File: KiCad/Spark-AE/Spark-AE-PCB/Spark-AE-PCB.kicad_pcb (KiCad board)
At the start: 2 copper layers, 50 x 100 mm, 100 parts, among them J1 Conn_01x20_Socket, J2 Conn_01x20_Socket, J3 AE_BUS, J4 Inputs, J5 Outputs, J6 I2C_IN, J7 I2C_OUT, J8 Conn_02x06_Top_Bottom, Q1 2N3904, Q2 2N3904, SW1 SW_Push, SW2 SW_Push, U2 MCP6002-xMS, U3 Driver_LED_PCA9633PW,118, U4 MCP6002-xMS, U5 MCP6002-xMS, U6 Connector_Micro_SD_Card_Yamai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, U7 MCP6002-xMS, U8 74LVC1G125

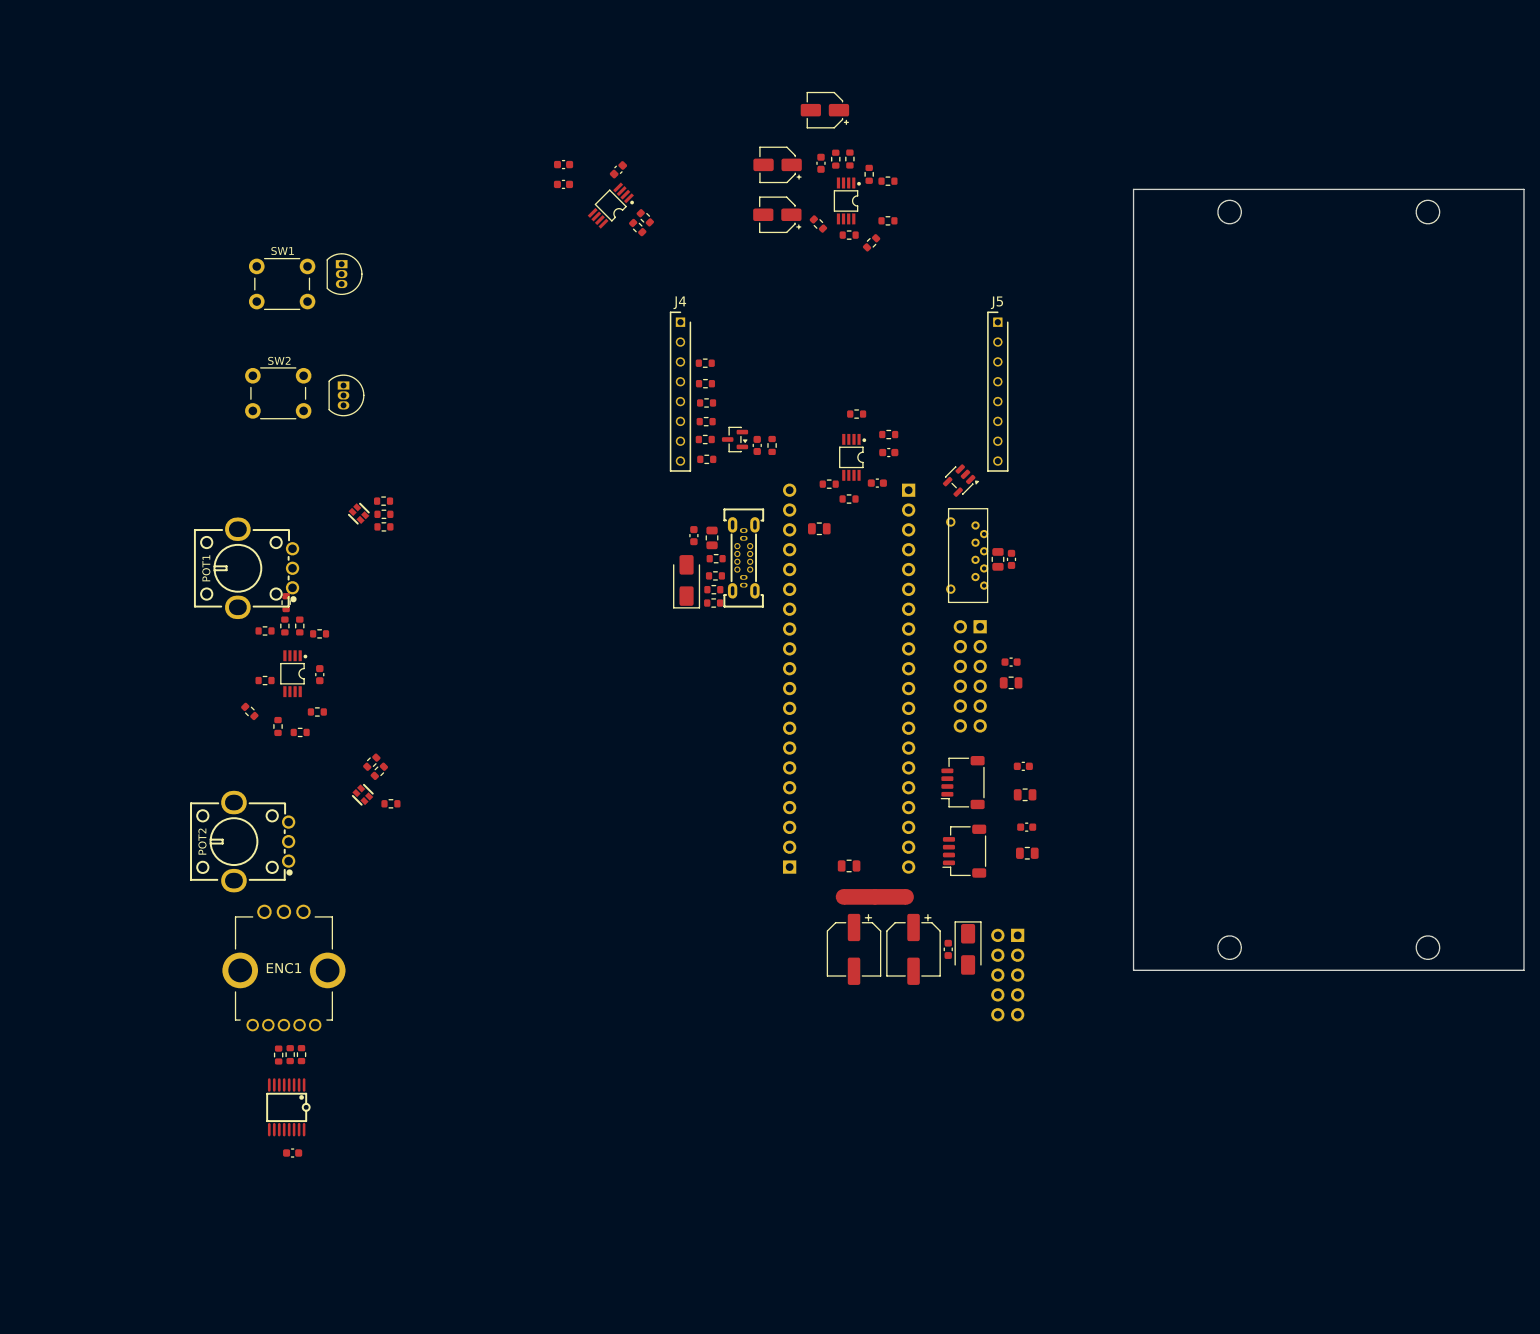
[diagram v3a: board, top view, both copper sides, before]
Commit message: schematic 100% complete. pcb layout around 50% complete.
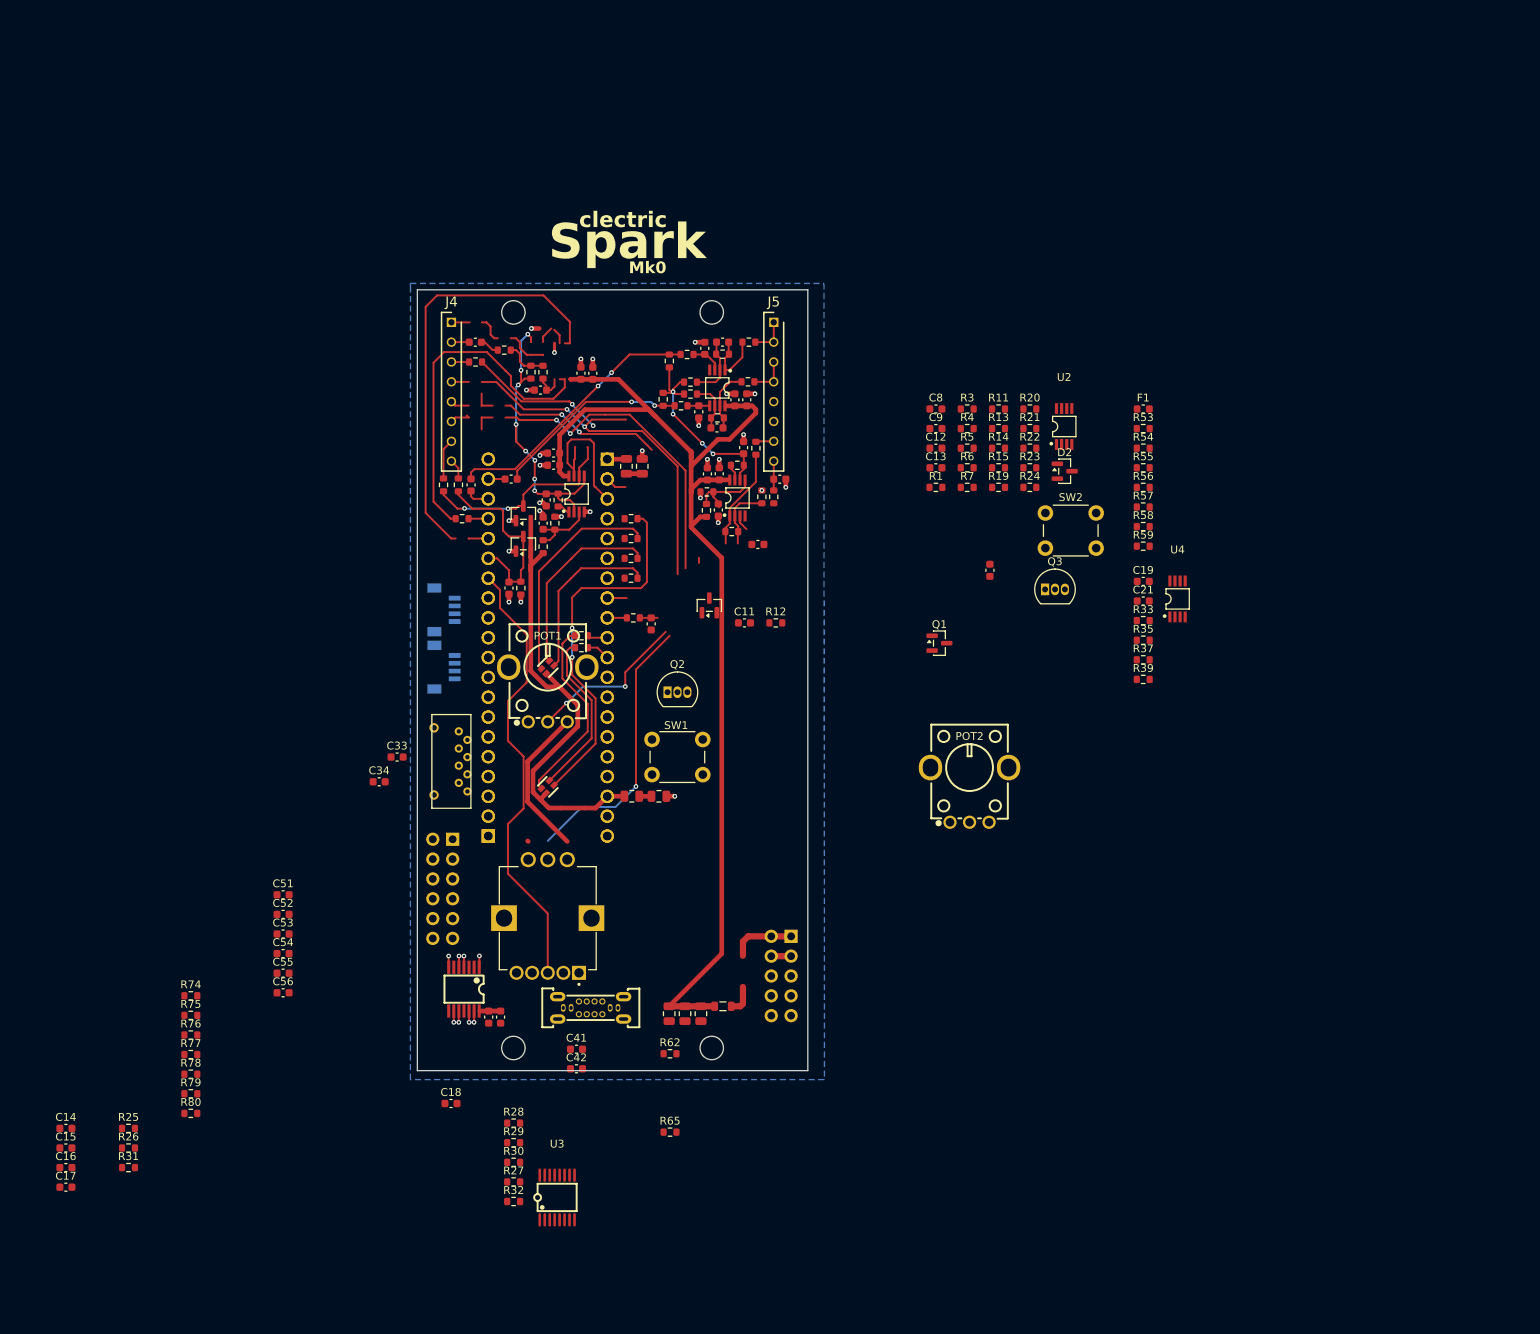
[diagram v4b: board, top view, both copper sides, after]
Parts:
- removed ENC1: RotaryEncoder_Switch_Bourns_PEL12T-4225S-S1024, clectric-diy:RotaryEncoder_Switch_Bourns_PEL12T-4225S-S1024
- removed J7: I2C_OUT, Connector_JST:JST_SH_SM04B-SRSS-TB_1x04-1MP_P1.00mm_Horizontal
- removed J8: Conn_02x06_Top_Bottom, Connector_PinHeader_2.54mm:PinHeader_2x06_P2.54mm_Vertical
- removed NT1: NetTie_3_Tee, NetTie:NetTie-3_SMD_Pad2.0mm
- added C27: 1nF, Capacitor_SMD:C_0603_1608Metric, F.Cu at (115.2, 53.6)
- added C28: 1nF, Capacitor_SMD:C_0603_1608Metric, F.Cu at (114.4, 61.8)
- added C29: 680pF, Capacitor_SMD:C_0603_1608Metric, F.Cu at (117.5, 52.8)
- added C30: 680pF, Capacitor_SMD:C_0603_1608Metric, F.Cu at (116.7, 63.8)
- added C31: 100nF, Capacitor_SMD:C_0603_1608Metric, F.Cu at (120.6, 60.2)
- added C32: 10uF, Capacitor_SMD:C_0603_1608Metric, F.Cu at (119.0, 60.2)
- added C33: 10uF, Capacitor_SMD:C_0603_1608Metric, F.Cu at (75.8, 106.0)
- added C34: 100nF, Capacitor_SMD:C_0603_1608Metric, F.Cu at (73.5, 109.1)
- added C35: 100nF, Capacitor_SMD:C_0603_1608Metric, F.Cu at (94.5, 76.0)
- added C36: 100nF, Capacitor_SMD:C_0603_1608Metric, F.Cu at (94.9, 73.1)
- added C37: 100nF, Capacitor_SMD:C_0603_1608Metric, F.Cu at (95.8, 68.6)
- added C38: 10uF, Capacitor_SMD:C_0603_1608Metric, F.Cu at (95.8, 67.1)
- added C39: 10nF, Capacitor_SMD:C_0603_1608Metric, F.Cu at (108.3, 88.9)
- added C40: 1nF, Capacitor_SMD:C_0603_1608Metric, F.Cu at (122.0, 78.8)
- added C41: 100nF, Capacitor_SMD:C_0603_1608Metric, F.Cu at (98.8, 143.4)
- added C42: 10uF, Capacitor_SMD:C_0603_1608Metric, F.Cu at (98.8, 145.9)
- added C43: 100nF, Capacitor_SMD:C_0603_1608Metric, F.Cu at (117.0, 69.7)
- added C44: 10uF, Capacitor_SMD:C_0603_1608Metric, F.Cu at (115.5, 69.7)
- added C45: 10pF, Capacitor_SMD:C_0603_1608Metric, F.Cu at (124.8, 70.4)
- added C46: 100nF, Capacitor_SMD:C_0603_1608Metric, F.Cu at (116.9, 74.3)
- added C47: 100pF, Capacitor_SMD:C_0603_1608Metric, F.Cu at (90.1, 84.3)
- added C48: 100nF, Capacitor_SMD:C_0603_1608Metric, F.Cu at (120.2, 66.4)
- added C49: 100nF, Capacitor_SMD:C_0603_1608Metric, F.Cu at (87.5, 139.3)
- added C50: 10uF, Capacitor_SMD:C_0603_1608Metric, F.Cu at (89.0, 139.3)
- added C51: 100nF, Capacitor_SMD:C_0603_1608Metric, F.Cu at (61.2, 123.6)
- added C52: 10uF, Capacitor_SMD:C_0603_1608Metric, F.Cu at (61.2, 126.1)
- added C53: 100nF, Capacitor_SMD:C_0603_1608Metric, F.Cu at (61.2, 128.6)
- added C54: 10uF, Capacitor_SMD:C_0603_1608Metric, F.Cu at (61.2, 131.1)
- added C55: 100nF, Capacitor_SMD:C_0603_1608Metric, F.Cu at (61.2, 133.7)
- added C56: 10uF, Capacitor_SMD:C_0603_1608Metric, F.Cu at (61.2, 136.2)
- added CN1: I2C_IN, clectric-diy:Connector_JST_BM04B-SRSS-TBT-LF-SN, B.Cu at (81.9, 87.1)
- added CN2: I2C_OUT, clectric-diy:Connector_JST_BM04B-SRSS-TBT-LF-SN, B.Cu at (81.8, 94.5)
- added D4: BAT54S, Package_TO_SOT_SMD:SOT-23, F.Cu at (91.9, 74.8)
- added D5: BAT54S, Package_TO_SOT_SMD:SOT-23, F.Cu at (91.9, 78.7)
- added F1: nSMD050-33V, Fuse:Fuse_0603_1608Metric, F.Cu at (171.3, 61.4)
- added Q3: 2N3904, Package_TO_SOT_THT:TO-92_Inline, F.Cu at (158.8, 84.5)
- added R11: 10K, Resistor_SMD:R_0603_1608Metric, F.Cu at (152.8, 61.4)
- added R22: 10K, Resistor_SMD:R_0603_1608Metric, F.Cu at (156.8, 66.4)
- added R47: 15K, Resistor_SMD:R_0603_1608Metric, F.Cu at (117.5, 54.4)
- added R48: 15K, Resistor_SMD:R_0603_1608Metric, F.Cu at (116.8, 62.5)
- added R49: 1K, Resistor_SMD:R_0603_1608Metric, F.Cu at (120.8, 52.8)
- added R50: 1K, Resistor_SMD:R_0603_1608Metric, F.Cu at (120.7, 57.9)
- added R51: 10K, Resistor_SMD:R_0603_1608Metric, F.Cu at (94.5, 79.0)
- added R52: 10K, Resistor_SMD:R_0603_1608Metric, F.Cu at (96.0, 76.0)
- added R53: 10K, Resistor_SMD:R_0603_1608Metric, F.Cu at (171.3, 63.9)
- added R54: 20K, Resistor_SMD:R_0603_1608Metric, F.Cu at (171.3, 66.4)
- added R55: 47K, Resistor_SMD:R_0603_1608Metric, F.Cu at (171.3, 68.9)
- added R56: 47K, Resistor_SMD:R_0603_1608Metric, F.Cu at (171.3, 71.4)
- added R57: 47K, Resistor_SMD:R_0603_1608Metric, F.Cu at (171.3, 74.0)
- added R58: 47K, Resistor_SMD:R_0603_1608Metric, F.Cu at (171.3, 76.5)
- added R59: 47K, Resistor_SMD:R_0603_1608Metric, F.Cu at (171.3, 79.0)
- added R60: 100R, Resistor_SMD:R_0603_1608Metric, F.Cu at (96.4, 73.1)
- added R61: 1K, Resistor_SMD:R_0603_1608Metric, F.Cu at (81.7, 71.1)
- added R62: 10K, Resistor_SMD:R_0603_1608Metric, F.Cu at (110.7, 144.0)
- added R63: 10K, Resistor_SMD:R_0603_1608Metric, F.Cu at (106.0, 88.2)
- added R64: 12.7K, Resistor_SMD:R_0603_1608Metric, F.Cu at (122.5, 72.7)
- added R65: 10K, Resistor_SMD:R_0603_1608Metric, F.Cu at (110.7, 154.0)
- added R66: 10K, Resistor_SMD:R_0603_1608Metric, F.Cu at (118.6, 77.1)
- added R67: 1K, Resistor_SMD:R_0603_1608Metric, F.Cu at (121.7, 66.4)
- added R68: 10K, Resistor_SMD:R_0603_1608Metric, F.Cu at (115.4, 74.4)
- added R69: 10K, Resistor_SMD:R_0603_1608Metric, F.Cu at (115.5, 72.0)
- added R70: 1K, Resistor_SMD:R_0603_1608Metric, F.Cu at (124.0, 72.7)
- added R71: 10K, Resistor_SMD:R_0603_1608Metric, F.Cu at (83.6, 71.1)
- added R72: 470R, Resistor_SMD:R_0603_1608Metric, F.Cu at (91.6, 84.3)
- added R73: 100R, Resistor_SMD:R_0603_1608Metric, F.Cu at (119.4, 68.6)
- added R74: 100R, Resistor_SMD:R_0603_1608Metric, F.Cu at (49.4, 136.5)
- added R75: 100R, Resistor_SMD:R_0603_1608Metric, F.Cu at (49.4, 139.1)
- added R76: 10K, Resistor_SMD:R_0603_1608Metric, F.Cu at (49.4, 141.6)
- added R77: 47R, Resistor_SMD:R_0603_1608Metric, F.Cu at (49.4, 144.1)
- added R78: 47R, Resistor_SMD:R_0603_1608Metric, F.Cu at (49.4, 146.6)
- added R79: 47R, Resistor_SMD:R_0603_1608Metric, F.Cu at (49.4, 149.1)
- added R80: 47R, Resistor_SMD:R_0603_1608Metric, F.Cu at (49.4, 151.6)
- added U1: Daisy_Seed, clectric-diy:MCU_Module_Electrosmith_DAISY_SEED, B.Cu at (87.5, 116.1)
- added U9: 74xx_Nexperia_74HCT125PW_118, clectric-diy:74xx_Nexperia_74HCT125PW_118, F.Cu at (84.3, 135.7)
- C1: value 220uF -> 100uF; footprint Capacitor_SMD:CP_Elec_6.3x5.4 -> Capacitor_SMD:C_0805_2012Metric
- C10: value 10uF -> 100nF; footprint Capacitor_SMD:CP_Elec_4x5.4 -> Capacitor_SMD:C_0603_1608Metric
- C11: footprint Capacitor_SMD:CP_Elec_4x5.4 -> Capacitor_SMD:C_0603_1608Metric
- C13: value 10uF -> 10nF; footprint Capacitor_SMD:CP_Elec_4x5.4 -> Capacitor_SMD:C_0603_1608Metric
- C14: value 10uF -> 10nF; footprint Capacitor_SMD:C_0805_2012Metric -> Capacitor_SMD:C_0603_1608Metric
- C15, C9: value 100nF -> 10nF
- C17, C25: value 100nF -> 10uF
- C19: value 100nF -> 1uF
- C2: value 220uF -> 10uF; footprint Capacitor_SMD:CP_Elec_6.3x5.4 -> Capacitor_SMD:C_0805_2012Metric
- C20: value 10uF -> 1uF; footprint Capacitor_SMD:C_0805_2012Metric -> Capacitor_SMD:C_0603_1608Metric
- C21: value 100nF -> 220pF
- C22: value 10uF -> 220pF; footprint Capacitor_SMD:C_0805_2012Metric -> Capacitor_SMD:C_0603_1608Metric
- C24, C26: footprint Capacitor_SMD:C_0805_2012Metric -> Capacitor_SMD:C_0603_1608Metric
- C3: value 10uF -> 100nF
- C5: footprint Capacitor_SMD:C_0603_1608Metric -> Capacitor_SMD:C_0805_2012Metric
- C6: value 100nF -> 10uF; footprint Capacitor_SMD:C_0603_1608Metric -> Capacitor_SMD:C_0805_2012Metric
- C7: value 1uF -> 100nF; footprint Capacitor_SMD:C_0603_1608Metric -> Capacitor_SMD:C_0805_2012Metric
- C8: value 1uF -> 100nF
- D1: value SS14 -> BAT54S; footprint Diode_SMD:D_SMA -> Package_TO_SOT_SMD:SOT-23
- D3: value 2214 -> RotaryEncoder_Switch_Bourns_PEL12T-4225S-S1024; footprint Diode_SMD:D_SMA -> clectric-diy:RotaryEncoder_Switch_Bourns_PEL12T-4225S-S1024
- FB1: value BLM18AG601 -> FerriteBead; footprint Inductor_SMD:L_0603_1608Metric -> Inductor_SMD:L_0805_2012Metric
- J6: value I2C_IN -> Conn_02x06_Top_Bottom; footprint Connector_JST:JST_SH_SM04B-SRSS-TB_1x04-1MP_P1.00mm_Horizontal -> Connector_PinHeader_2.54mm:PinHeader_2x06_P2.54mm_Vertical; moved to B.Cu
- Q1: value 2N3904 -> AO3401; footprint Package_TO_SOT_THT:TO-92_Inline -> Package_TO_SOT_SMD:SOT-23
- R1, R13, R38: value 1K8 -> 10K
- R10, R18: value 100K -> 47R
- R12: value 10K -> 1K
- R14, R41, R42, R6: value 1K -> 100K
- R15, R25, R7: value 100R -> 10K
- R16, R8: value 100R -> 47R
- R17: value 3K3 -> 330R
- R19: value 100K -> 10K
- R2: value 3K3 -> 10K
- R23: value 1K -> 10K
- R24: value 100R -> 1K
- R26: value 4K7 -> 10K
- R28: value 100K -> 680R
- R29: value 100K -> 470R
- R30: value 10K -> 470R
- R32: value 100K -> 4K7
- R33: value 100K -> 150K
- R34: value 15K -> 150K
- R35: value 15K -> 100K
- R36: value 10K -> 100K
- R39: value 3K3 -> 1K
- R40: value 5K1 -> 1K
- R45, R46: value 5K1 -> 10K
- R9: value 100K -> 330R
- U2, U4, U5: value MCP6002-xMS -> MCP6002T-I_MS
- U6: value Connector_Micro_SD_Card_Yamaichi_PJS008U-3000-0 -> MCP6002T-I_MS; footprint clectric-diy:PJS008U-3000-0 -> clectric-diy:Amplifier_Operational_Microchip_MCP6002T-I_MS
- U7: value MCP6002-xMS -> Connector_Micro_SD_Card_Yamaichi_PJS008U-3000-0; footprint clectric-diy:Amplifier_Operational_Microchip_MCP6002T-I_MS -> clectric-diy:PJS008U-3000-0
- U8: value 74LVC1G125 -> MCP6002T-I_MS; footprint Package_TO_SOT_SMD:SOT-23-5 -> clectric-diy:Amplifier_Operational_Microchip_MCP6002T-I_MS
- moved R31 149.7 mm to (41.4, 158.5), turned to 0 degrees
- moved C15 142.6 mm to (33.4, 156.0), turned to 0 degrees
- moved C14 139.8 mm to (33.4, 153.5), turned to 0 degrees
- moved R32 139.2 mm to (90.7, 162.9), turned to 0 degrees
- moved C17 137.6 mm to (33.4, 161.1), turned to 0 degrees
- moved R30 134.9 mm to (90.7, 157.9), turned to 0 degrees
- moved R26 134.7 mm to (41.4, 156.0), turned to 0 degrees
- moved R28 130.8 mm to (90.7, 152.9), turned to 0 degrees
- moved C16 128.0 mm to (33.4, 158.5), turned to 0 degrees
- moved R27 124.6 mm to (90.7, 160.4), turned to 0 degrees
- moved R29 123.9 mm to (90.7, 155.4), turned to 0 degrees
- moved R23 119.8 mm to (156.8, 68.9), turned to 0 degrees
- moved R24 119.4 mm to (156.8, 71.4), turned to 0 degrees
- moved U2 103.8 mm to (161.2, 63.6), turned to 0 degrees
- moved R21 101.2 mm to (156.8, 63.9)
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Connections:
- C1 pad 1: 5V -> +5V
- C10 pad 1: Net-(U5A-+) -> +5V
- C10 pad 2: AUDIO_OUT_1 -> GND
- C11 pad 1: Net-(U5B-+) -> GND
- C11 pad 2: AUDIO_OUT_2 -> +5V
- C12 pad 1: GNDA -> SW2
- C12 pad 2: 5V -> GND
- C13 pad 1: 5V -> POT2
- C13 pad 2: GNDA -> GND
- C14 pad 1: 3V3_D -> ENC_A
- C14 pad 2: GNDD -> GND
- C15 pad 1: 3V3_D -> ENC_B
- C15 pad 2: GNDD -> GND
- C16 pad 1: A1_D16 -> GND
- C16 pad 2: GNDA -> ENC_CLICK
- C17 pad 1: GNDA -> +3.3V
- C17 pad 2: 5V -> GND
- C18 pad 1: GNDD -> +3.3V
- C18 pad 2: 5V -> GND
- C19 pad 1: GNDD -> AUDIO_AE_IN_1
- C19 pad 2: 5V -> Net-(C19-Pad2)
- C2 pad 1: 5V -> +5V
- C20 pad 1: GNDD -> AUDIO_AE_IN_2
- C20 pad 2: 5V -> Net-(C20-Pad2)
- C21 pad 1: 3V3_D -> Net-(U4A-+)
- C21 pad 2: GNDD -> GND
- C22 pad 1: 3V3_D -> Net-(U4B-+)
- C22 pad 2: GNDD -> GND
- C23 pad 1: 3V3_D -> GND
- C23 pad 2: GNDD -> +5V
- C24 pad 1: 3V3_D -> GND
- C24 pad 2: GNDD -> +5V
- C25 pad 1: 3V3_D -> Net-(C25-Pad1)
- C25 pad 2: GNDD -> AUDIO_OUT_1
- C26 pad 1: 3V3_D -> Net-(C26-Pad1)
- C26 pad 2: GNDD -> AUDIO_OUT_2
- C3 pad 1: 3V3_D -> +5V
- C3 pad 2: GNDD -> GND
- C4 pad 1: 3V3_A -> +3.3V
- C4 pad 2: GNDA -> Net-(C4-Pad2)
- C5 pad 1: GNDA -> Net-(C4-Pad2)
- C5 pad 2: 3V3_D -> GND
- C6 pad 1: GNDD -> +3.3VA
- C6 pad 2: 3V3_D -> Net-(C6-Pad2)
- C7 pad 1: AUDIO_AE_IN_1 -> Net-(C6-Pad2)
- C7 pad 2: Net-(U4A-+) -> GND
- C8 pad 1: AUDIO_AE_IN_2 -> SW1
- C8 pad 2: Net-(U4B-+) -> GND
- C9 pad 1: GNDA -> POT1
- C9 pad 2: 5V -> GND
- D1 pad 1: 5V -> GND
- D1 pad 2: GND -> +3.3VA
- D2 pad 1: GNDA -> GND
- D2 pad 2: 3V3_D -> +3.3VA
- D2 pad 3: A1_D16 -> POT2
- D3 pad 1: 5V -> Net-(D3-Pad1)
- D3 pad 2: GNDD -> Net-(D3-Pad2)
- FB1 pad 1: 5V -> +5V
- FB1 pad 2: GND -> /Power Regulation/VCC_PROTECT
- J1 pad 1: 3V3_A -> +3.3VA
- J1 pad 18: 3V3_D -> +3.3V
- J1 pad 19: 5V -> +5V
- J1 pad 20: GNDD -> GND
- J1 pad 3: A1_D16 -> A1
- J1 pad 9: A7_D22 -> A7
- J2 pad 20: GNDA -> GND
- J3 pad 1: 5V -> /Power Regulation/VCC_RAW
- J3 pad 2: 5V -> /Power Regulation/VCC_RAW
- J4 pad 7: A1_D16_AE_IN -> A1_AE_IN
- J5 pad 7: A7_D22_AE_OUT -> A7_AE_OUT
- J6 pad 1: 3V3_D -> Net-(J6-Pin_1)
- J6 pad 2: GNDD -> Net-(J6-Pin_2)
- J6 pad 3: I2C_SDA -> Net-(J6-Pin_3)
- J6 pad 4: I2C_SCL -> Net-(J6-Pin_4)
- LED1 pad 3: 3V3_D -> +3.3V
- LED2 pad 3: 3V3_D -> +3.3V
- POT1 pad 1: 3V3_A -> GND
- POT1 pad 3: GNDA -> +3.3VA
- POT1 pad 4: GNDA -> GND
- POT1 pad 5: GNDA -> GND
- POT2 pad 1: 3V3_A -> GND
- POT2 pad 3: GNDA -> +3.3VA
- POT2 pad 4: GNDA -> GND
- POT2 pad 5: GNDA -> GND
- Q1 pad 1: GNDD -> GND
- Q1 pad 2: Net-(Q1-B) -> /Power Regulation/VCC_PROTECT
- Q1 pad 3: SW_1 -> /Power Regulation/VCC_RAW
- Q2 pad 1: GNDD -> GND
- Q2 pad 3: SW_2 -> SW1
- R1 pad 2: Net-(R1-Pad2) -> GND
- R10 pad 1: Net-(U2A--) -> LED1_B
- R10 pad 2: POT1 -> Net-(LED1-Pad4)
- R12 pad 1: SW2_CV -> Net-(R11-Pad2)
- R12 pad 2: Net-(Q2-B) -> POT1
- R13 pad 2: Net-(R13-Pad2) -> GND
- R14 pad 1: LED2_G -> Net-(U2B-+)
- R14 pad 2: Net-(LED2-Pad1) -> POT2_CV
- R15 pad 1: LED2_B -> SW2_CV
- R15 pad 2: Net-(LED2-Pad2) -> Net-(Q3-B)
- R16 pad 1: LED2_R -> LED2_G
- R16 pad 2: Net-(LED2-Pad4) -> Net-(LED2-Pad1)
- R17 pad 1: Net-(R13-Pad2) -> LED2_R
- R17 pad 2: GNDA -> Net-(LED2-Pad2)
- R18 pad 1: Net-(R13-Pad2) -> LED2_B
- R18 pad 2: Net-(U2B-+) -> Net-(LED2-Pad4)
- R19 pad 1: GNDA -> +3.3V
- R19 pad 2: Net-(U2B--) -> SW2
- R2 pad 1: Net-(R1-Pad2) -> SW1_CV
- R2 pad 2: GNDA -> Net-(Q2-B)
- R20 pad 1: Net-(U2B-+) -> Net-(POT2-Pad2)
- R20 pad 2: Net-(POT2-Pad2) -> Net-(U2B-+)
- R21 pad 1: Net-(U2B--) -> Net-(Q3-B)
- R21 pad 2: POT2 -> GND
- R23 pad 1: Net-(ENC1--_1) -> Net-(U2B--)
- R23 pad 2: ENC_LED_RED -> Net-(R23-Pad2)
- R24 pad 1: Net-(ENC1--_2) -> Net-(R23-Pad2)
- R24 pad 2: ENC_LED_GREEN -> POT2
- R25 pad 1: Net-(ENC1-+_1) -> +3.3V
- R25 pad 2: ENC_LED_BLUE -> ENC_A
- R26 pad 1: 3V3_D -> +3.3V
- R26 pad 2: I2C_SDA -> ENC_B
- R27 pad 1: 3V3_D -> +3.3V
- R27 pad 2: I2C_SCL -> I2C_SDA
- R28 pad 1: Net-(U4B--) -> Net-(D3-Pad1)
- R28 pad 2: AUDIO_IN_2 -> ENC_LED_RED
- R29 pad 1: Net-(U4A--) -> Net-(D3-Pad2)
- R29 pad 2: AUDIO_IN_1 -> ENC_LED_GREEN
- R3 pad 1: SW1_CV -> +3.3V
- R3 pad 2: Net-(Q1-B) -> SW1
- R30 pad 1: 5V -> Net-(D3-Pad4)
- R30 pad 2: Net-(U5A--) -> ENC_LED_BLUE
- R31 pad 1: 5V -> +3.3V
- R31 pad 2: Net-(U5B--) -> ENC_CLICK
- R32 pad 1: 5V -> +3.3V
- R32 pad 2: Net-(U5A-+) -> I2C_SCL
- R33 pad 1: 5V -> Net-(C19-Pad2)
- R33 pad 2: Net-(U5B-+) -> Net-(R33-Pad2)
- R34 pad 1: Net-(U5A--) -> Net-(C20-Pad2)
- R35 pad 1: Net-(U5B--) -> Net-(R33-Pad2)
- R35 pad 2: Net-(R35-Pad2) -> VREF_1V65
- R36 pad 2: AUDIO_AE_OUT_1 -> VREF_1V65
- R37 pad 1: Net-(R35-Pad2) -> Net-(R33-Pad2)
- R37 pad 2: AUDIO_AE_OUT_2 -> Net-(U4A-+)
- R38 pad 1: A1_D16 -> Net-(R34-Pad2)
- R38 pad 2: A1_D16_AE_IN -> Net-(U4B-+)
- R39 pad 1: A1_D16 -> AUDIO_IN_1
- R39 pad 2: GNDA -> Net-(U4A--)
- R4 pad 1: Net-(R1-Pad2) -> Net-(U2A-+)
- R4 pad 2: Net-(U2A-+) -> POT1_CV
- R40 pad 1: GNDA -> AUDIO_IN_2
- R40 pad 2: Net-(R40-Pad2) -> Net-(U4B--)
- R41 pad 1: D14_AE_IN -> VREF_2V5
- R41 pad 2: D14 -> Net-(C25-Pad1)
- R42 pad 1: Net-(R40-Pad2) -> VREF_2V5
- R42 pad 2: A7_D22_AE_OUT -> Net-(C26-Pad1)
- R43 pad 1: Net-(U7B-+) -> Net-(C25-Pad1)
- R43 pad 2: 5V -> Net-(U5A-+)
- R44 pad 1: GNDA -> Net-(C26-Pad1)
- R44 pad 2: Net-(U7B-+) -> Net-(U5B-+)
- R45 pad 1: GNDD -> VREF_2V5
- R45 pad 2: Net-(USB1-CC1) -> Net-(U5A--)
- R46 pad 1: Net-(USB1-CC2) -> VREF_2V5
- R46 pad 2: GNDD -> Net-(U5B--)
- R5 pad 1: GNDA -> Net-(Q2-B)
- R5 pad 2: Net-(U2A--) -> GND
- R6 pad 1: LED1_G -> Net-(POT1-Pad2)
- R6 pad 2: Net-(LED1-Pad1) -> Net-(U2A-+)
- R7 pad 1: LED1_B -> Net-(U2A--)
- R7 pad 2: Net-(LED1-Pad2) -> GND
- R8 pad 1: LED1_R -> LED1_G
- R8 pad 2: Net-(LED1-Pad4) -> Net-(LED1-Pad1)
- R9 pad 1: Net-(U2A-+) -> LED1_R
- R9 pad 2: Net-(POT1-Pad2) -> Net-(LED1-Pad2)
- SW1 pad 1: SW_1 -> SW1
- SW1 pad 2: GNDD -> GND
- SW2 pad 1: SW_2 -> SW2
- SW2 pad 2: GNDD -> GND
- U2 pad 1: POT1 -> Net-(R11-Pad2)
- U2 pad 4: GNDA -> GND
- U2 pad 7: POT2 -> Net-(R23-Pad2)
- U2 pad 8: 3V3_D -> +5V
- U3 pad 1: GNDD -> GND
- U3 pad 10: GNDD -> GND
- U3 pad 11: GNDD -> GND
- U3 pad 14: GNDD -> GND
- U3 pad 15: GNDD -> GND
- U3 pad 16: 3V3_D -> +3.3V
- U3 pad 2: GNDD -> GND
- U3 pad 7: GNDD -> GND
- U3 pad 8: GNDD -> GND
- U3 pad 9: GNDD -> GND
- U4 pad 4: GNDA -> GND
- U4 pad 8: 5V -> +5V
- U5 pad 1: Net-(R34-Pad2) -> Net-(C29-Pad1)
- U5 pad 4: GNDA -> GND
- U5 pad 7: Net-(R35-Pad2) -> Net-(C30-Pad1)
- U5 pad 8: 5V -> +5V
- U8 pad 1: GNDD -> Net-(C40-Pad1)
- U8 pad 2: D0_AE_OUT -> Net-(U8A--)
- U8 pad 3: GNDD -> Net-(U8A-+)
- U8 pad 4: D0 -> GND
- U8 pad 5: 5V -> Net-(U8B-+)
- USB1 pad 17: GNDD -> GND
- USB1 pad 18: GNDD -> GND
- USB1 pad 19: GNDD -> GND
- USB1 pad 20: GNDD -> GND
- USB1 pad A12B1: GNDD -> GND
- USB1 pad A1B12: GNDD -> GND
- USB1 pad A4B9: 5V -> Net-(C41-Pad2)
- USB1 pad A9B4: 5V -> Net-(C41-Pad2)
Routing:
- net +5V: track 0.00 -> 147.9 mm
- net Net-(Q2-B): track 0.00 -> 66.7 mm, vias 0 -> 4
- net +3.3V: track 0.00 -> 60.3 mm, vias 0 -> 1
- net ENC_CLICK: track 0.00 -> 57.3 mm
- net Net-(U4A--): track 0.00 -> 55.5 mm
- net Net-(LED2-Pad2): track 0.00 -> 46.9 mm, vias 0 -> 2
- net Net-(U4B--): track 0.00 -> 44.4 mm
- net VREF_1V65: track 0.00 -> 41.2 mm, vias 0 -> 10
- net GND: track 0.00 -> 40.5 mm, vias 0 -> 35
- net Net-(U2B-+): track 0.00 -> 40.4 mm, vias 0 -> 2
- net (no net): track 0.00 -> 39.3 mm
- net Net-(POT2-Pad2): track 0.00 -> 35.3 mm, vias 0 -> 1
- net Net-(C25-Pad1): track 0.00 -> 33.9 mm, vias 0 -> 2
- net Net-(LED1-Pad4): track 0.00 -> 28.4 mm
- net VREF_2V5: track 0.00 -> 26.0 mm, vias 0 -> 4
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- added copper zone on B.Cu, net GND
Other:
- board text added: "Mk0"
- board text added: "Spark"
- board text added: "clectric"

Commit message: continuing to plug away at pcb layout
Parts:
- removed the C6 at (105.1, 68.7)
- removed the C7 at (107.2, 68.7)
- C4: footprint Capacitor_SMD:C_0805_2012Metric -> Capacitor_SMD:C_0603_1608Metric
- C5: value 100nF -> 10uF; footprint Capacitor_SMD:C_0805_2012Metric -> Capacitor_SMD:C_0603_1608Metric
- R51, R52, R68, R69: value 10K -> 100K
- U1: moved to F.Cu
- moved U1 116.4 mm to (28.6, 15.7)
- moved C17 91.7 mm to (85.8, 50.3)
- moved R33 89.4 mm to (89.5, 52.5), turned to -90 degrees
- moved R39 89.0 mm to (84.2, 78.0), turned to 180 degrees
- moved R35 86.9 mm to (92.9, 53.7), turned to -90 degrees
- moved R37 86.6 mm to (94.5, 53.7), turned to 90 degrees
- moved R53 85.6 mm to (85.7, 65.6)
- moved U4 84.5 mm to (96.9, 55.3), turned to 180 degrees
- moved C19 84.1 mm to (94.8, 51.1), turned to 180 degrees
- moved R54 82.6 mm to (88.8, 64.8), turned to 90 degrees
- moved R21 71.4 mm to (85.8, 56.5), turned to 180 degrees
- moved R15 67.9 mm to (85.8, 58.0)
- moved R14 67.1 mm to (85.8, 62.5), turned to 180 degrees
- moved R13 67.0 mm to (85.8, 64.1)
- moved SW2 64.5 mm to (108.4, 115.1)
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- renumbered C12 to C10, C13 to C11, C14 to C12, C15 to C13, C16 to C14, C17 to C15, C18 to C16, C19 to C17, C20 to C18, C21 to C19, C22 to C20, C23 to C21, C24 to C22, C25 to C23, C26 to C24, C27 to C25, C28 to C26, C29 to C27, C30 to C28, C31 to C29, C32 to C30, C33 to C31, C34 to C32, C35 to C33, C36 to C34, C37 to C35, C38 to C36, C39 to C37, C40 to C38, C41 to C39, C42 to C40, C43 to C41, C44 to C42, C45 to C43, C46 to C44, C47 to C45, C48 to C46, C49 to C47, C50 to C48, C51 to C49, C52 to C50, C53 to C51, C54 to C52, C55 to C53, C56 to C54, C8 to C6, C9 to C7, C10 to C8, C11 to C9
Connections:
- C4 pad 1: +3.3V -> GND
- C4 pad 2: Net-(C4-Pad2) -> +3.3V
- C5 pad 1: Net-(C4-Pad2) -> GND
- C5 pad 2: GND -> +3.3VA
- R61 pad 1: A1 -> Net-(D4-COM)
- R61 pad 2: Net-(D4-COM) -> A1
- R73 pad 1: Net-(U8B--) -> Net-(R73-Pad1)
- U8 pad 6: Net-(U8B--) -> VREF_2V5
- U8 pad 7: Net-(U8B--) -> Net-(R73-Pad1)
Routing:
- net Net-(Q3-B): track 0.00 -> 92.7 mm, vias 0 -> 2
- net +3.3VA: track 21.9 -> 73.6 mm
- net (no net): track 39.3 -> 0.00 mm
- net ENC_B: track 0.00 -> 35.5 mm
- net Net-(POT2-Pad2): track 35.3 -> 0.00 mm, vias 1 -> 0
- net ENC_A: track 0.00 -> 33.4 mm
- net +5V: track 147.9 -> 173.6 mm
- net Net-(POT1-Pad2): track 21.0 -> 0.00 mm, vias 2 -> 0
- net Net-(U8A-+): track 4.42 -> 24.3 mm, vias 0 -> 2
- net Net-(U4B--): track 44.4 -> 63.9 mm
- net Net-(D4-COM): track 0.00 -> 19.4 mm, vias 0 -> 2
- net SW2: track 0.00 -> 18.8 mm
- net Net-(U2B-+): track 40.4 -> 22.0 mm
- net VREF_1V65: track 41.2 -> 25.1 mm, vias 10 -> 4
- net A1: track 20.0 -> 4.32 mm
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
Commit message: I accdently upgraded to KiCad 10 via a `brew upgrade`. I committing before launching it just in case.
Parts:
- removed C39: 100nF, Capacitor_SMD:C_0603_1608Metric
- removed C40: 10uF, Capacitor_SMD:C_0603_1608Metric
- removed F1: nSMD050-33V, Fuse:Fuse_0603_1608Metric
- removed U1: Daisy_Seed, clectric-diy:MCU_Module_Electrosmith_DAISY_SEED
- added C55: 100nF, Capacitor_SMD:C_0603_1608Metric, F.Cu at (107.6, 143.4)
- added C56: 10uF, Capacitor_SMD:C_0603_1608Metric, F.Cu at (109.1, 143.4)
- added F2: nSMD050-33V, Fuse:Fuse_0603_1608Metric, F.Cu at (110.6, 143.4)
- C49, C50, C51, C52, R74, R75: moved to B.Cu
- CN1, CN2: moved to F.Cu
- R62, R65: value 10K -> 56K
- U9: value 74xx_Nexperia_74HCT125PW_118 -> 74xGxx_MDD_74AHCT1G125GV; footprint clectric-diy:74xx_Nexperia_74HCT125PW_118 -> clectric-diy:74xGxx_MDD_74AHCT1G125GV
- USB1: value USB_C_Receptacle_G-Switch_GT-USB-7038A -> USB_C_Receptacle_H8.8mm_Jing_918-648K2027E30002; footprint clectric-diy:USB_C_Receptacle_G-Switch_GT-USB-7038A -> clectric-diy:USB_C_Receptacle_H8.8mm_Jing_918-648K2027E30002
- moved R32 75.2 mm to (90.8, 87.7), turned to 180 degrees
- moved R27 74.2 mm to (90.8, 86.2), turned to 180 degrees
- moved C43 62.9 mm to (79.8, 114.3), turned to -90 degrees
- moved R70 59.7 mm to (81.3, 114.3)
- moved C15 53.5 mm to (83.0, 140.9)
- moved U7 50.5 mm to (60.8, 111.7), turned to -90 degrees
- moved R74 49.2 mm to (65.4, 90.0), turned to 180 degrees
- moved R75 49.2 mm to (65.4, 92.6), turned to 180 degrees
- moved C49 43.8 mm to (65.4, 80.0), turned to 180 degrees
- moved C50 43.8 mm to (65.4, 82.5), turned to 180 degrees
- moved C51 43.8 mm to (65.4, 85.0), turned to 180 degrees
- moved C52 43.8 mm to (65.4, 87.5), turned to 180 degrees
- moved R62 42.9 mm to (101.4, 135.8)
- moved USB1 40.7 mm to (103.4, 139.1), turned to 0 degrees
- moved CN2 37.2 mm to (81.7, 97.8)
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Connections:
- R62 pad 1: Net-(C39-Pad2) -> Net-(C55-Pad1)
- R65 pad 1: Net-(USB1-CC2) -> Net-(C55-Pad1)
- R65 pad 2: Net-(C39-Pad2) -> Net-(USB1-CC2)
- R70 pad 2: Net-(U9-1Y) -> Net-(U9-Y)
- U9 pad 3: Net-(U9-1Y) -> GND
- U9 pad 4: GND -> Net-(U9-Y)
- U9 pad 5: GND -> +5V
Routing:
- net Net-(POT1-Pad2): track 0.00 -> 88.0 mm, vias 0 -> 6
- net Net-(POT2-Pad2): track 0.00 -> 76.9 mm, vias 0 -> 4
- net POT1_CV: track 3.98 -> 51.6 mm, vias 0 -> 4
- net +3.3V: track 64.8 -> 111.5 mm, vias 0 -> 2
- net USB_D-: track 0.00 -> 46.2 mm, vias 0 -> 4
- net USB_D+: track 0.00 -> 44.3 mm, vias 0 -> 4
- net POT2_CV: track 3.94 -> 47.0 mm, vias 0 -> 4
- net POT2: track 0.00 -> 33.7 mm
- net Net-(C55-Pad1): track 0.00 -> 31.6 mm
- net +5V: track 173.6 -> 203.7 mm
- net +3.3VA: track 73.6 -> 103.6 mm, vias 0 -> 2
- net Net-(U8A-+): track 24.3 -> 0.00 mm, vias 2 -> 0
- net A7: track 2.20 -> 24.6 mm, vias 0 -> 3
- net Net-(U2A-+): track 26.4 -> 5.30 mm, vias 2 -> 0
- net POT1: track 2.04 -> 23.1 mm, vias 0 -> 2
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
